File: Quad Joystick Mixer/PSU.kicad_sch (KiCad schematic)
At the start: 58 parts, among them J1 Barrel_Jack_Switch, SW1 SW_DPDT_x2, U1 LM338-TO-220, U2 LM2990T-12/NOPB, U3 AP63200WU

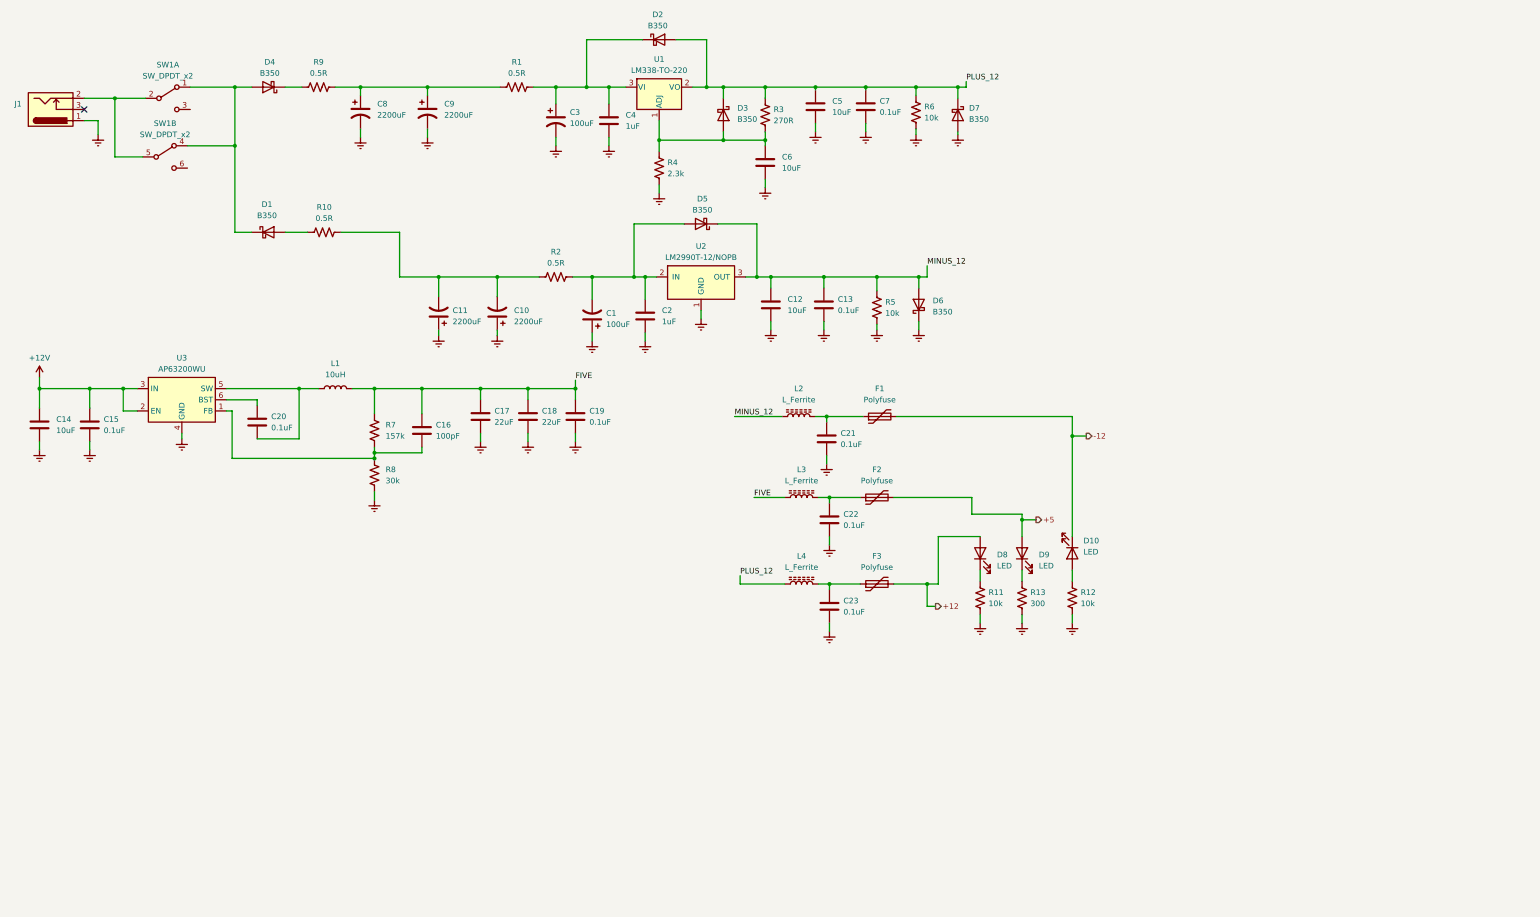
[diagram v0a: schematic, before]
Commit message: add analog 5V rail
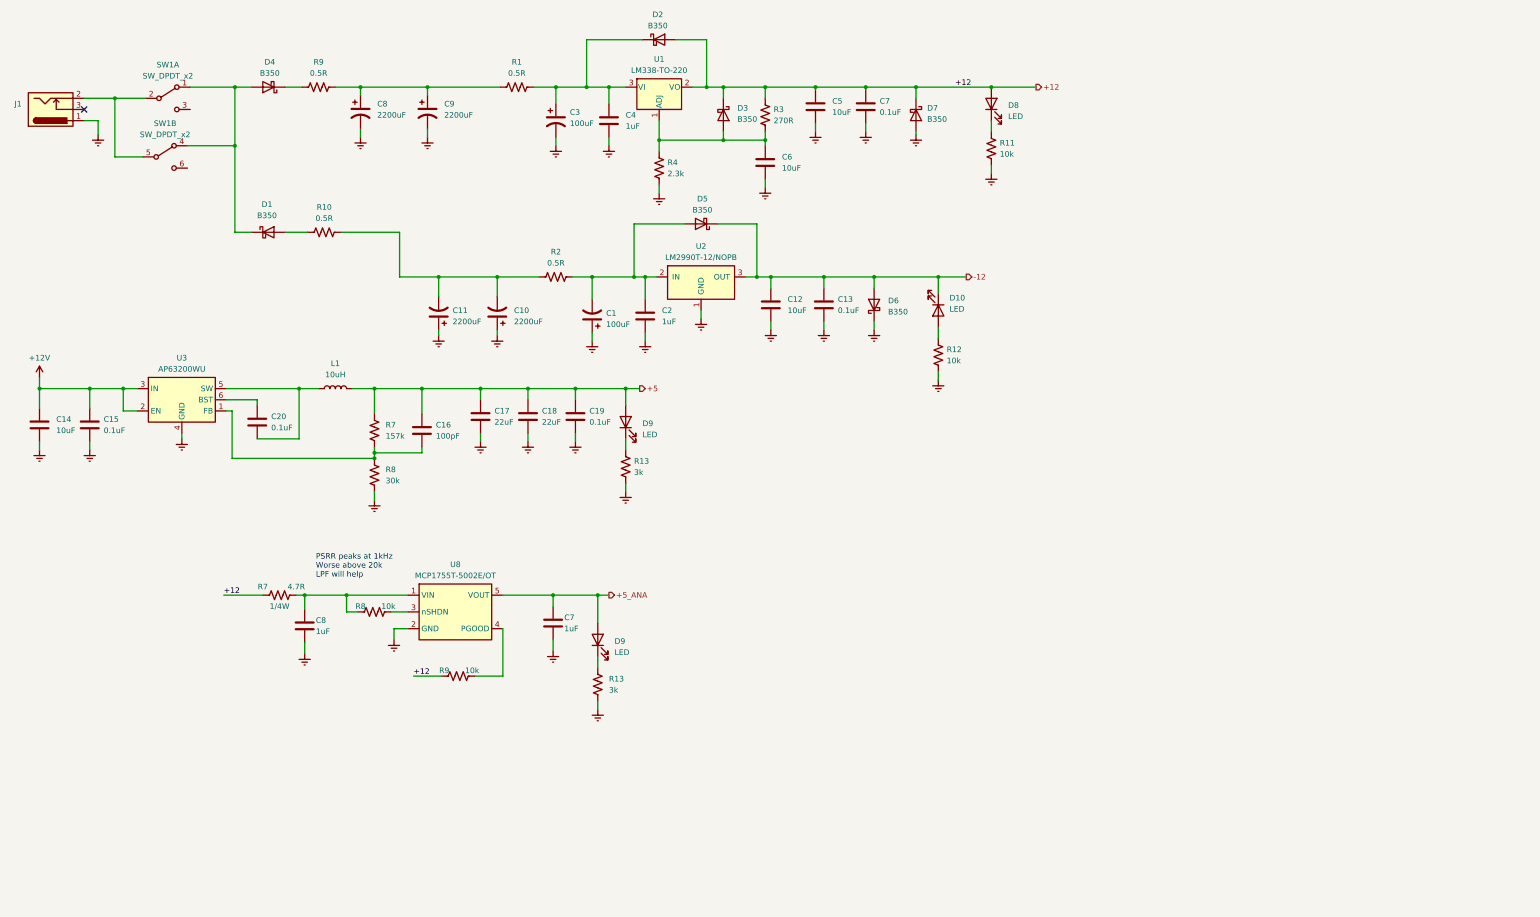
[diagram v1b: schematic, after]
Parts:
- removed C21, C22, C23: 0.1uF, Capacitor_SMD:C_0805_2012Metric_Pad1.18x1.45mm_HandSolder, symbol Device:C
- removed F1, F2, F3: Polyfuse, Fuse:Fuse_1206_3216Metric_Pad1.42x1.75mm_HandSolder, symbol Device:Polyfuse
- removed L2, L3, L4: L_Ferrite, Inductor_SMD:L_0805_2012Metric_Pad1.15x1.40mm_HandSolder, symbol Device:L_Ferrite
- removed R5, R6: 10k, Resistor_SMD:R_0805_2012Metric_Pad1.20x1.40mm_HandSolder, symbol Device:R_US
- added C7, C8: 1uF, Capacitor_SMD:C_0805_2012Metric_Pad1.18x1.45mm_HandSolder, symbol Device:C
- added D9: LED, LED_THT:LED_D3.0mm_FlatTop, symbol Device:LED
- added R13: 3k, Resistor_SMD:R_0805_2012Metric_Pad1.20x1.40mm_HandSolder, symbol Device:R_US
- added R7: 4.7R, Resistor_SMD:R_2010_5025Metric_Pad1.40x2.65mm_HandSolder, symbol Device:R_US
- added R8, R9: 10k, Resistor_SMD:R_0805_2012Metric_Pad1.20x1.40mm_HandSolder, symbol Device:R_US
- added U8: MCP1755T-5002E/OT, Package_TO_SOT_SMD:SOT-23-5_HandSoldering, symbol Eyewool ICs:MCP1755T-5002E/OT
- R13: value 300 -> 3k
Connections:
- net FIVE is gone; now on net +5: C16.1, C17.1, C18.1, C19.1, L1.2, R7.1
- net MINUS_12 is gone; now on net -12: C12.1, C13.1, D5.1 (K), D6.2 (A), U2.3 (OUT)
- net PLUS_12 is gone; now on net +12: C5.1, C7.1, D2.2 (A), D3.1 (K), D7.1 (K), R3.1, U1.2 (VO)
- net +12: now also R7.1, R9.1
- net Earth: now also C7.2, C8.2, R13.2, U8.2 (GND)
- new net: D9.1 (K), R13.1
- new net: C8.1, R7.2, R8.1, U8.1 (VIN)
- new net: R8.2, U8.3 (nSHDN)
- new net: R9.2, U8.4 (PGOOD)
- new net +5_ANA: C7.1, D9.2 (A), U8.5 (VOUT)
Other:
- note added: "PSRR peaks at 1kHz Worse above 20k LPF will help"
- moved on the sheet: D10, D6, D7, D8, D9, R11, R12, R13

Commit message: add in rotary circuit and some docs
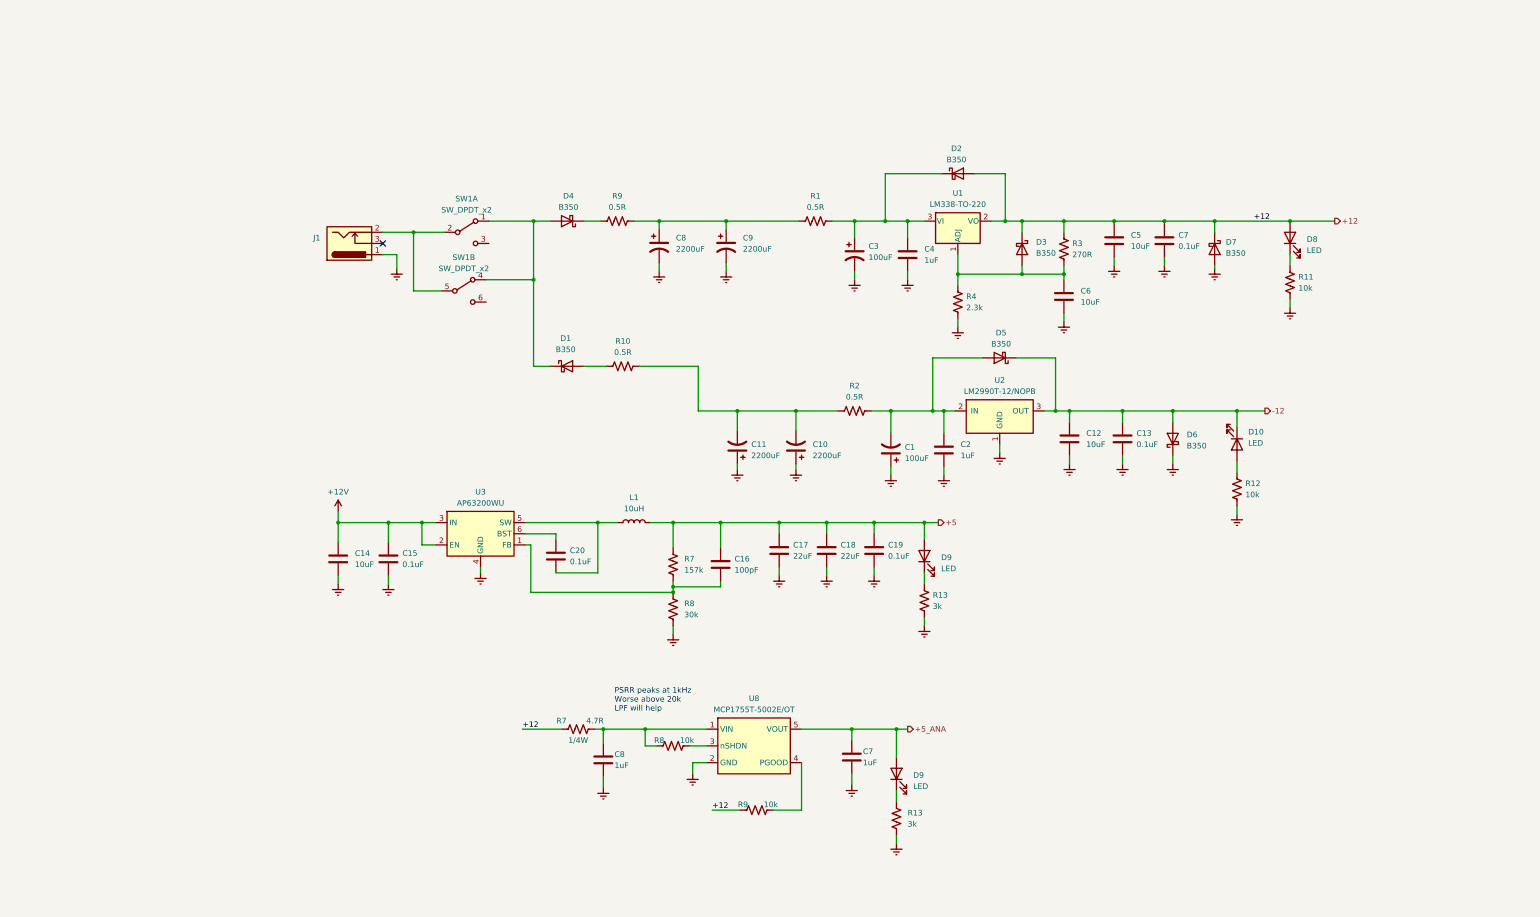
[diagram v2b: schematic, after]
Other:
- moved on the sheet: C1, C10, C11, C12, C13, C14, C15, C16, C17, C18, C19, C2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

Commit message: finished first draft of the schematic
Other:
- note added: "Power Supplies"
- title: (none) -> Quadrophonic Joystick Mixer
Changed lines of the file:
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@@
   (paper "B")
   (title_block
+    (title "Quadrophonic Joystick Mixer")
     (date "2024-02-14")
+    (rev "P1")
   )
   (junction (at 219.075 105.41) (diameter 0) (color 0 0 0 0)
@@
     (stroke (width 0) (type default))
   )
+  (text "Power Supplies" (at 170.18 34.29 0)
+    (effects (font (size 3.81 3.81) (thickness 0.508) bold) (justify left bottom))
+  )
   (text "PSRR peaks at 1kHz\nWorse above 20k\nLPF will help" (at 156.21 173.99 0)

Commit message: ok the draft wasn't done but now i think it is
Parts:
- added TP1 (x4): TestPoint, TestPoint:TestPoint_THTPad_D1.5mm_Drill0.7mm, symbol Connector:TestPoint
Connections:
- net +12: now also TP1.1
- net +5: now also TP1.1
- net +5_ANA: now also TP1.1
- net -12: now also TP1.1
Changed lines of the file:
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@@
     (rev "P1")
   )
+  (junction (at 222.885 130.81) (diameter 0) (color 0 0 0 0)
+  )
   (junction (at 219.075 105.41) (diameter 0) (color 0 0 0 0)
   )
   (junction (at 169.545 145.415) (diameter 0) (color 0 0 0 0)
   )
+  (junction (at 300.99 105.41) (diameter 0) (color 0 0 0 0)
+  )
   (junction (at 153.67 177.8) (diameter 0) (color 0 0 0 0)
   )
@@
   (junction (at 169.545 146.685) (diameter 0) (color 0 0 0 0)
   )
+  (junction (at 217.17 177.8) (diameter 0) (color 0 0 0 0)
+  )
   (junction (at 309.88 62.23) (diameter 0) (color 0 0 0 0)
   )
@@
   (junction (at 269.875 62.23) (diameter 0) (color 0 0 0 0)
   )
+  (junction (at 315.595 62.23) (diameter 0) (color 0 0 0 0)
+  )
   (junction (at 166.37 62.23) (diameter 0) (color 0 0 0 0)
   )
@@
   )
   (no_connect (at 103.505 67.31))
+  (wire (pts (xy 300.99 105.41) (xy 304.165 105.41))
+    (stroke (width 0) (type default))
+  )
   (wire (pts (xy 241.935 62.23) (xy 245.11 62.23))
     (stroke (width 0) (type default))
@@
     (stroke (width 0) (type default))
   )
-  (wire (pts (xy 215.265 130.81) (xy 226.695 130.81))
+  (wire (pts (xy 215.265 130.81) (xy 222.885 130.81))
     (stroke (width 0) (type default))
   )
@@
     (stroke (width 0) (type default))
   )
+  (wire (pts (xy 300.99 102.87) (xy 300.99 105.41))
+    (stroke (width 0) (type default))
+  )
   (wire (pts (xy 144.145 177.8) (xy 135.255 177.8))
     (stroke (width 0) (type default))
@@
     (stroke (width 0) (type default))
   )
-  (wire (pts (xy 309.88 62.23) (xy 320.04 62.23))
+  (wire (pts (xy 309.88 62.23) (xy 315.595 62.23))
     (stroke (width 0) (type default))
   )
@@
     (stroke (width 0) (type default))
   )
+  (wire (pts (xy 220.345 173.355) (xy 217.17 173.355))
+    (stroke (width 0) (type default))
+  )
   (wire (pts (xy 228.6 93.345) (xy 228.6 105.41))
     (stroke (width 0) (type default))
@@
     (stroke (width 0) (type default))
   )
-  (wire (pts (xy 297.815 105.41) (xy 304.165 105.41))
+  (wire (pts (xy 297.815 105.41) (xy 300.99 105.41))
     (stroke (width 0) (type default))
   )
@@
     (stroke (width 0) (type default))
   )
+  (wire (pts (xy 222.885 127.635) (xy 222.885 130.81))
+    (stroke (width 0) (type default))
+  )
   (wire (pts (xy 248.92 74.295) (xy 258.445 74.295))
     (stroke (width 0) (type default))
@@
     (stroke (width 0) (type default))
   )
+  (wire (pts (xy 217.17 173.355) (xy 217.17 177.8))
+    (stroke (width 0) (type default))
+  )
   (wire (pts (xy 197.485 105.41) (xy 207.01 105.41))
     (stroke (width 0) (type default))
@@
     (stroke (width 0) (type default))
   )
+  (wire (pts (xy 224.79 127.635) (xy 222.885 127.635))
+    (stroke (width 0) (type default))
+  )
   (wire (pts (xy 175.26 105.41) (xy 184.15 105.41))
     (stroke (width 0) (type default))
@@
     (stroke (width 0) (type default))
   )
+  (wire (pts (xy 217.17 177.8) (xy 210.185 177.8))
+    (stroke (width 0) (type default))
+  )
   (wire (pts (xy 169.545 145.415) (xy 169.545 144.145))
     (stroke (width 0) (type default))
@@
     (stroke (width 0) (type default))
   )
-  (wire (pts (xy 220.345 177.8) (xy 210.185 177.8))
+  (wire (pts (xy 220.345 177.8) (xy 217.17 177.8))
     (stroke (width 0) (type default))
   )
@@
     (stroke (width 0) (type default))
   )
+  (wire (pts (xy 315.595 62.23) (xy 320.04 62.23))
+    (stroke (width 0) (type default))
+  )
   (wire (pts (xy 142.875 142.24) (xy 152.4 142.24))
     (stroke (width 0) (type default))
@@
     (stroke (width 0) (type default))
   )
+  (wire (pts (xy 315.595 59.69) (xy 315.595 62.23))
+    (stroke (width 0) (type default))
+  )
   (wire (pts (xy 210.185 177.8) (xy 210.185 180.34))
     (stroke (width 0) (type default))
@@
   )
   (wire (pts (xy 152.4 130.81) (xy 156.845 130.81))
+    (stroke (width 0) (type default))
+  )
+  (wire (pts (xy 222.885 130.81) (xy 226.695 130.81))
     (stroke (width 0) (type default))
   )
@@
     )
   )
+  (symbol (lib_id "Connector:TestPoint") (at 220.345 173.355 270) (unit 1)
+    (in_bom yes) (on_board yes) (dnp no) (fields_autoplaced)
+    (property "Reference" "TP1" (at 226.06 173.355 90)
+      (effects (font (size 1.27 1.27)) (justify left))
+    )
+    (property "Value" "TestPoint" (at 222.377 175.26 0)
+      (effects (font (size 1.27 1.27)) (justify left) hide)
+    )
+    (property "Footprint" "TestPoint:TestPoint_THTPad_D1.5mm_Drill0.7mm" (at 220.345 178.435 0)
+      (effects (font (size 1.27 1.27)) hide)
+    )
+    (property "Datasheet" "~" (at 220.345 178.435 0)
+      (effects (font (size 1.27 1.27)) hide)
+    )
+    (pin "1")
+    (instances
+      (project "Quad Joystick Mixer"
+        (path "/e9da4955-68c1-4335-ab8e-8a9cc0328d2d/70e873e8-c2f7-42de-91d7-3f147d0d972e"
+          (reference "TP1") (unit 1)
+        )
+        (path "/e9da4955-68c1-4335-ab8e-8a9cc0328d2d/547597e7-7fd4-4461-bc12-6ec4a58ef011"
+          (reference "TP5") (unit 1)
+        )
+      )
+    )
+  )
   (symbol (lib_id "power:Earth") (at 258.445 85.09 0) (unit 1)
     (in_bom yes) (on_board yes) (dnp no) (fields_autoplaced)
@@
     )
   )
+  (symbol (lib_id "Connector:TestPoint") (at 300.99 102.87 0) (unit 1)
+    (in_bom yes) (on_board yes) (dnp no) (fields_autoplaced)
+    (property "Reference" "TP1" (at 303.53 99.568 0)
+      (effects (font (size 1.27 1.27)) (justify left))
+    )
+    (property "Value" "TestPoint" (at 302.895 100.838 0)
+      (effects (font (size 1.27 1.27)) (justify left) hide)
+    )
+    (property "Footprint" "TestPoint:TestPoint_THTPad_D1.5mm_Drill0.7mm" (at 306.07 102.87 0)
+      (effects (font (size 1.27 1.27)) hide)
+    )
+    (property "Datasheet" "~" (at 306.07 102.87 0)
+      (effects (font (size 1.27 1.27)) hide)
+    )
+    (pin "1")
+    (instances
+      (project "Quad Joystick Mixer"
+        (path "/e9da4955-68c1-4335-ab8e-8a9cc0328d2d/70e873e8-c2f7-42de-91d7-3f147d0d972e"
+          (reference "TP1") (unit 1)
+        )
+        (path "/e9da4955-68c1-4335-ab8e-8a9cc0328d2d/547597e7-7fd4-4461-bc12-6ec4a58ef011"
+          (reference "TP3") (unit 1)
+        )
+      )
+    )
+  )
+  (symbol (lib_id "Connector:TestPoint") (at 224.79 127.635 270) (unit 1)
+    (in_bom yes) (on_board yes) (dnp no) (fields_autoplaced)
+    (property "Reference" "TP1" (at 230.505 127.635 90)
+      (effects (font (size 1.27 1.27)) (justify left))
+    )
+    (property "Value" "TestPoint" (at 226.822 129.54 0)
+      (effects (font (size 1.27 1.27)) (justify left) hide)
+    )
+    (property "Footprint" "TestPoint:TestPoint_THTPad_D1.5mm_Drill0.7mm" (at 224.79 132.715 0)
+      (effects (font (size 1.27 1.27)) hide)
+    )
+    (property "Datasheet" "~" (at 224.79 132.715 0)
+      (effects (font (size 1.27 1.27)) hide)
+    )
+    (pin "1")
+    (instances
+      (project "Quad Joystick Mixer"
+        (path "/e9da4955-68c1-4335-ab8e-8a9cc0328d2d/70e873e8-c2f7-42de-91d7-3f147d0d972e"
+          (reference "TP1") (unit 1)
+        )
+        (path "/e9da4955-68c1-4335-ab8e-8a9cc0328d2d/547597e7-7fd4-4461-bc12-6ec4a58ef011"
+          (reference "TP4") (unit 1)
+        )
+      )
+    )
+  )
   (symbol (lib_id "Device:C_Polarized_US") (at 181.61 67.945 0) (unit 1)
     (in_bom yes) (on_board yes) (dnp no) (fields_autoplaced)
@@
         )
       )
+    )
+  )
+  (symbol (lib_id "Connector:TestPoint") (at 315.595 59.69 0) (unit 1)
+    (in_bom yes) (on_board yes) (dnp no) (fields_autoplaced)
+    (property "Reference" "TP1" (at 318.135 56.388 0)
+      (effects (font (size 1.27 1.27)) (justify left))
+    )
+    (property "Value" "TestPoint" (at 317.5 57.658 0)
+      (effects (font (size 1.27 1.27)) (justify left) hide)
+    )
+    (property "Footprint" "TestPoint:TestPoint_THTPad_D1.5mm_Drill0.7mm" (at 320.675 59.69 0)
+      (effects (font (size 1.27 1.27)) hide)
+    )
+    (property "Datasheet" "~" (at 320.675 59.69 0)
+      (effects (font (size 1.27 1.27)) hide)
+    )
+    (pin "1")
+    (instances
+      (project "Quad Joystick Mixer"
+        (path "/e9da4955-68c1-4335-ab8e-8a9cc0328d2d/70e873e8-c2f7-42de-91d7-3f147d0d972e"
+          (reference "TP1") (unit 1)
+        )
+        (path "/e9da4955-68c1-4335-ab8e-8a9cc0328d2d/547597e7-7fd4-4461-bc12-6ec4a58ef011"
+          (reference "TP2") (unit 1)
+        )
+      )

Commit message: clean up after review, working through BOM
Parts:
- C7, C8: DK PN (none) -> 1276-1029-1-ND; MPN C28323 -> CL21B105KBFNNNE
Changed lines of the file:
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@@
       (effects (font (size 1.27 1.27)) hide)
     )
-    (property "MPN" "C28323" (at 153.67 184.785 0)
+    (property "MPN" "CL21B105KBFNNNE" (at 153.67 184.785 0)
+      (effects (font (size 1.27 1.27)) hide)
+    )
+    (property "DK PN" "1276-1029-1-ND" (at 153.67 184.785 0)
       (effects (font (size 1.27 1.27)) hide)
     )
@@
       (effects (font (size 1.27 1.27)) hide)
     )
-    (property "MPN" "C28323" (at 210.185 184.15 0)
-      (effects (font (size 1.27 1.27)) hide)
-    )
+    (property "MPN" "CL21B105KBFNNNE" (at 210.185 184.15 0)
+      (effects (font (size 1.27 1.27)) hide)
+    )
+    (property "DK PN" "1276-1029-1-ND" (at 210.185 184.15 0)
+      (effects (font (size 1.27 1.27)) hide)
+    )

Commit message: finish adding parts to the BOM
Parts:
- C1, C10, C11, C12, C13, C14, C15, C16, C17, C18, C19, C2, C20, C3, C4, C5, C6, C7, C8, C9, D1, D2, D3, D4, D5, D6, D7, L1, R1, R10, R2, R9: Source (none) -> DK
- D10, D8, D9, J1, SW1: Source (none) -> SBP
- R11, R12: DK PN (none) -> RMCF0805JT10K0CT-ND; MPN (none) -> RMCF0805JT10K0; Source (none) -> DK
- R13: DK PN (none) -> A126368CT-ND; MPN (none) -> CRG0805F3K0; Source (none) -> DK
- R3: DK PN (none) -> 311-270CRCT-ND; MPN (none) -> RC0805FR-07270RL; Source (none) -> DK
- R4: value 2.3k -> 2.32k; DK PN (none) -> RMCF0805FT2K32CT-ND; MPN (none) -> RMCF0805FT2K32; Source (none) -> DK
- R7: value 157k -> 158k; DK PN (none) -> 311-158KCRCT-ND; MPN (none) -> RES 158K OHM 1% 1/8W 0805; Source (none) -> DK
- R7: DK PN (none) -> RMCF2010FT4R70CT-ND; MPN (none) -> RMCF2010FT4R70; Power 1/4W -> 3/4W; Source (none) -> DK
- R8: DK PN (none) -> RMCF0805JT30K0CT-ND; MPN (none) -> RMCF0805JT30K0; Source (none) -> DK
- R8, R9: DK PN (none) -> RMCF0805JT10K0CT-ND; MPN C17414 -> RMCF0805JT10K0; Source (none) -> DK
- TP1: Source (none) -> NA
- U1: DK PN (none) -> LM338T/NOPB-ND; MPN (none) -> LM338T/NOPB; Source (none) -> DK
- U2: DK PN (none) -> LM2990T-12/NOPB-ND; MPN (none) -> LM2990T-12/NOPB; Source (none) -> DK
- U3: DK PN (none) -> AP63200WU-7; MPN (none) -> AP63200WU-7DICT-ND; Source (none) -> DK
- U8: DK PN (none) -> MCP1755T-5002E/OT; MPN (none) -> MCP1755T-5002E/OTCT-ND; Source (none) -> DK

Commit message: major layout progress
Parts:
- added C16, C34, C36, C60: 0.1uF, Capacitor_SMD:C_0805_2012Metric_Pad1.18x1.45mm_HandSolder, symbol Device:C
- added R23, R8: 20k, Resistor_SMD:R_0805_2012Metric_Pad1.20x1.40mm_HandSolder, symbol Device:R_US
- added TP1: TestPoint, TestPoint:TestPoint_THTPad_D1.5mm_Drill0.7mm, symbol Connector:TestPoint
- added U4: TL072, Package_SO:SOIC-8_3.9x4.9mm_P1.27mm, symbol Amplifier_Operational:OPA1692xD
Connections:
- net +12: now also R7.2; no longer R7.1
- net +12V: now also C16.1, U4.8 (V+)
- net +5_ANA: now also C36.1, R8.1
- net Earth: no longer C7.2, C8.2, R13.2, U8.2 (GND)
- net at C8.1, R8.1, U8.1 (VIN): now also R7.1; no longer R7.2
- new net: R23.1, R8.2, U4.3 (+), U4.5 (+)
- new net -12V: C34.1, U4.4 (V-)
- new net GND: C16.2, C34.2, C36.2, C60.2, C7.2, C8.2, R13.2, R23.2, U8.2 (GND)
- new net VDD: C60.1, TP1.1, U4.1, U4.2 (-), U4.6 (-), U4.7
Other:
- moved on the sheet: R7
